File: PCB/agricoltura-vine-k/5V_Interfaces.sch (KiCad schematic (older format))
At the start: 8 parts, among them T19 TSW-108-07-G-T, U8 TCA6416ARTWR

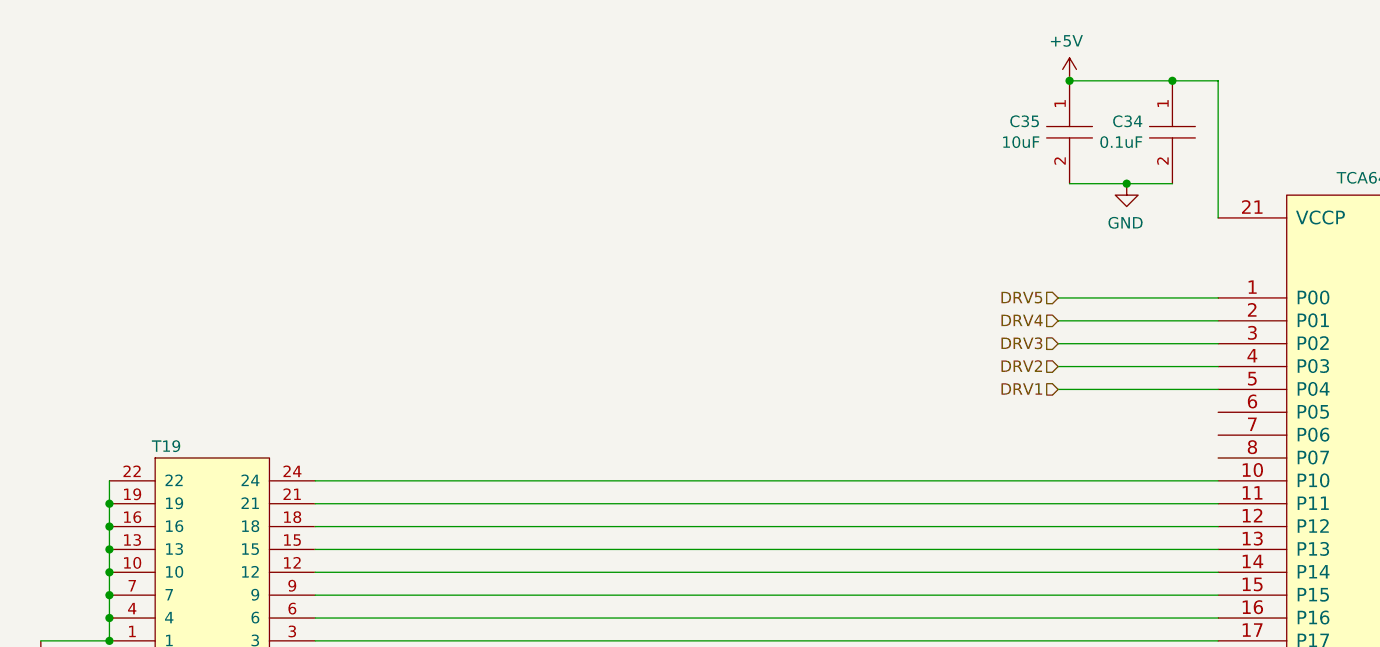
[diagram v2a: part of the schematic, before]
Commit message: EEPROM
added EEPROM to IO expander serial port. Broke out remaining IO expander pins to header. Adjusted silkscreen labeling and reset button position to match the other Vine.
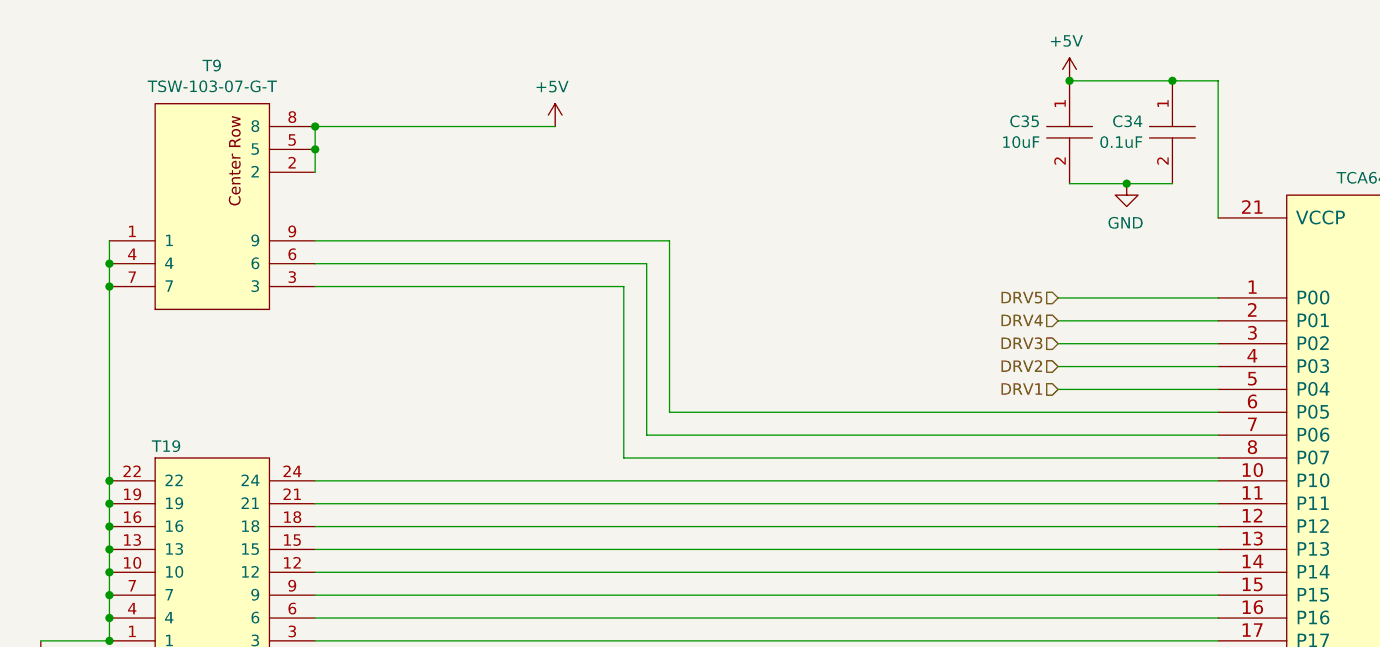
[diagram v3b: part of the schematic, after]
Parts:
- added T9: TSW-103-07-G-T, AVR-KiCAD-Lib-Connectors:TSW-103-07-G-T, symbol AVR-KiCAD-Lib-Connectors:TSW-103-07-G-T
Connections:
- net +5V: now also T9.2, T9.5, T9.8
- net GND: now also T9.1, T9.4, T9.7
- net at U8.6 (P05): now also T9.9
- net at U8.7 (P06): now also T9.6
- net at U8.8 (P07): now also T9.3
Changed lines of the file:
@@
 Wire Wire Line
 	7450 4900 6750 4900
+$Comp
+L AVR-KiCAD-Lib-Connectors:TSW-103-07-G-T T9
+U 1 1 5F29B8F0
+P 2800 4550
+F 0 "T9" H 3050 3485 50  0000 C CNN
+F 1 "TSW-103-07-G-T" H 3050 3576 50  0000 C CNN
+F 2 "AVR-KiCAD-Lib-Connectors:TSW-103-07-G-T" H 2600 4550 50  0001 C CNN
+F 3 "http://suddendocs.samtec.com/catalog_english/tsw_th.pdf" H 2700 4650 50  0001 C CNN
+F 4 "1.01000" H 2900 4800 50  0001 C CNN "Cost QTY: 1"
+F 5 "0.55680" H 3000 4900 50  0001 C CNN "Cost QTY: 1000"
+F 6 "*" H 3100 5000 50  0001 C CNN "Cost QTY: 2500"
+F 7 "0.48720" H 3200 5100 50  0001 C CNN "Cost QTY: 5000"
+F 8 "0.46284" H 3300 5200 50  0001 C CNN "Cost QTY: 10000"
+F 9 "Samtec Inc." H 3400 5300 50  0001 C CNN "MFR"
+F 10 "TSW-103-07-G-T" H 3500 5400 50  0001 C CNN "MFR#"
+F 11 "Digikey" H 3600 5500 50  0001 C CNN "Vendor"
+F 12 "SAM10328-ND" H 3700 5600 50  0001 C CNN "Vendor #"
+F 13 "AVR" H 3800 5700 50  0001 C CNN "Designer"
+F 14 "10.92mm" H 3900 5800 50  0001 C CNN "Height"
+F 15 "7/23/2020" H 5000 6900 50  0001 C CNN "Date Created"
+F 16 "7/23/2020" H 4000 5900 50  0001 C CNN "Date Modified"
+F 17 "Yes" H 4100 6000 50  0001 C CNN "Lead-Free ?"
+F 18 "1" H 4200 6100 50  0001 C CNN "RoHS Levels"
+F 19 "ThroughHole" H 4300 6200 50  0001 C CNN "Mounting"
+F 20 "96" H 4400 6300 50  0001 C CNN "Pin Count #"
+F 21 "Active" H 4500 6400 50  0001 C CNN "Status"
+F 22 "*" H 4600 6500 50  0001 C CNN "Tolerance"
+F 23 "Connector" H 4700 6600 50  0001 C CNN "Type"
+F 24 "*" H 4800 6700 50  0001 C CNN "Voltage"
+F 25 "*" H 4900 6850 50  0001 C CNN "Package"
+F 26 "Connector Header Through Hole 9 position 0.100\" (2.54mm)" H 5300 7250 50  0001 C CNN "Description"
+F 27 "3X03" H 5100 7050 50  0001 C CNN "_Value_"
+F 28 "*" H 5200 7150 50  0001 C CNN "Management_ID"
+	1    2800 4550
+	1    0    0    1
+$EndComp
+Wire Wire Line
+	7450 5000 5050 5000
+Wire Wire Line
+	5050 5000 5050 4250
+Wire Wire Line
+	5050 4250 3500 4250
+Wire Wire Line
+	4950 4350 4950 5100
+Wire Wire Line
+	4950 5100 7450 5100
+Wire Wire Line
+	7450 5200 4850 5200
+Wire Wire Line
+	4850 5200 4850 4450
+Wire Wire Line
+	4850 4450 3500 4450
+Wire Wire Line
+	3500 4350 4950 4350
+Connection ~ 2600 5300
+Wire Wire Line
+	2600 4250 2600 4350
+Wire Wire Line
+	3500 3950 3500 3850
+Connection ~ 3500 3850
+Wire Wire Line
+	3500 3850 3500 3750
+Wire Wire Line
+	3500 3750 4550 3750
+Connection ~ 3500 3750
+Connection ~ 2600 4350
+Wire Wire Line
+	2600 4350 2600 4450
+Connection ~ 2600 4450
+Wire Wire Line
+	2600 4450 2600 5300
+$Comp
+L power:+5V #PWR?
+U 1 1 5F2BACA7
+P 4550 3750
+F 0 "#PWR?" H 4550 3600 50  0001 C CNN
+F 1 "+5V" H 4565 3923 50  0000 C CNN
+F 2 "" H 4550 3750 50  0001 C CNN
+F 3 "" H 4550 3750 50  0001 C CNN
+	1    4550 3750
+	-1   0    0    -1
+$EndComp
 $EndSCHEMATC
